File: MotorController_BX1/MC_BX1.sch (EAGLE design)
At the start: 6 parts

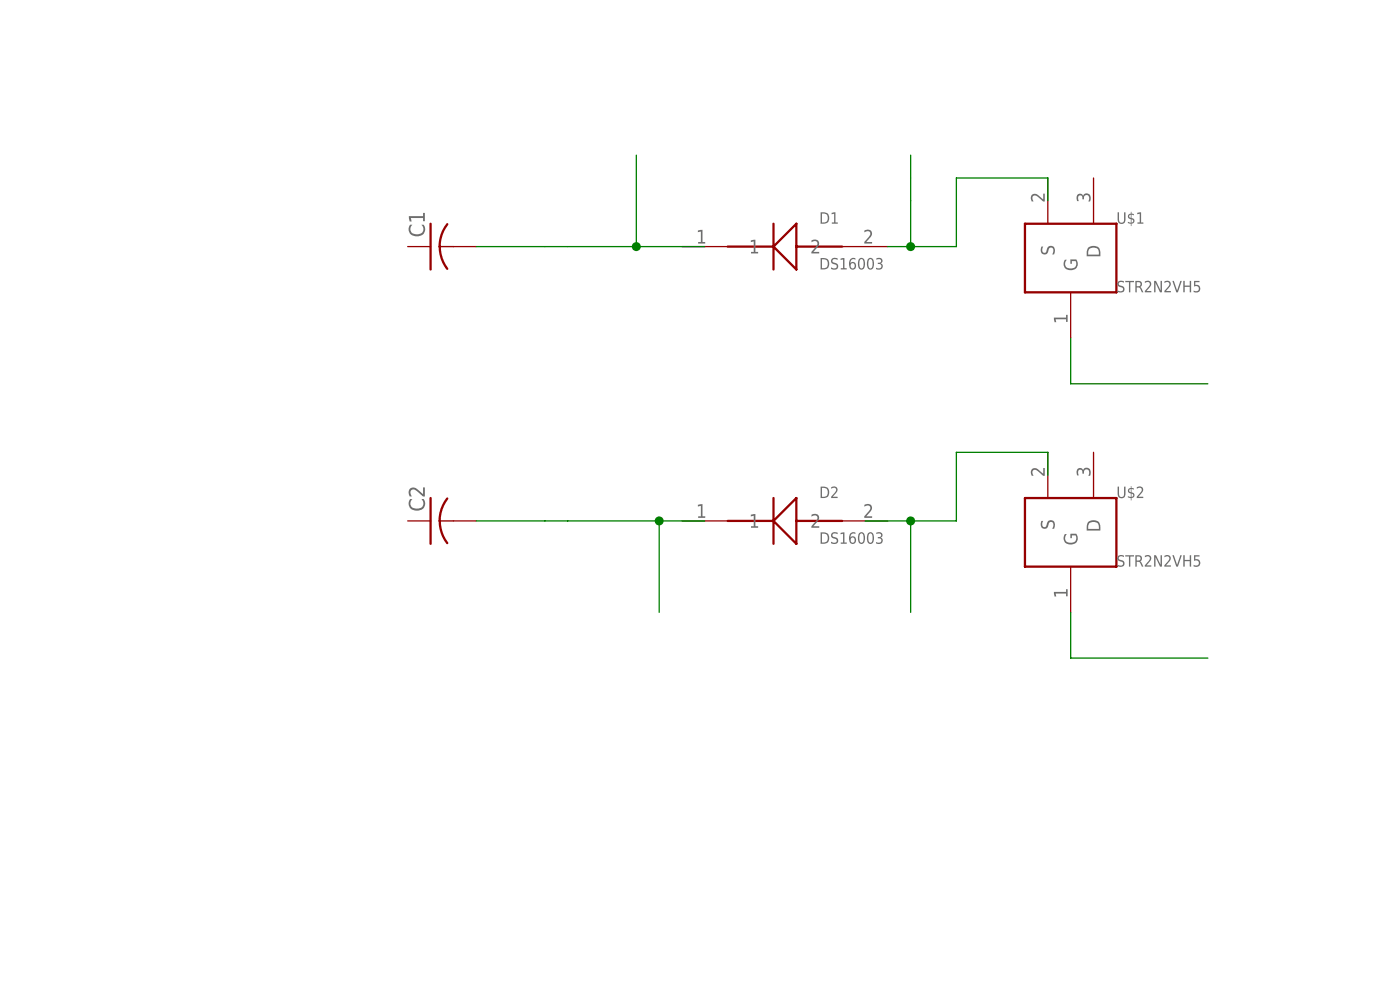
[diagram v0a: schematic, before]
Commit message: Finished first revision of motor controller schematic. Pending: zener shunted to ground, C1 value, and decoupling capacitors from PWM to GND
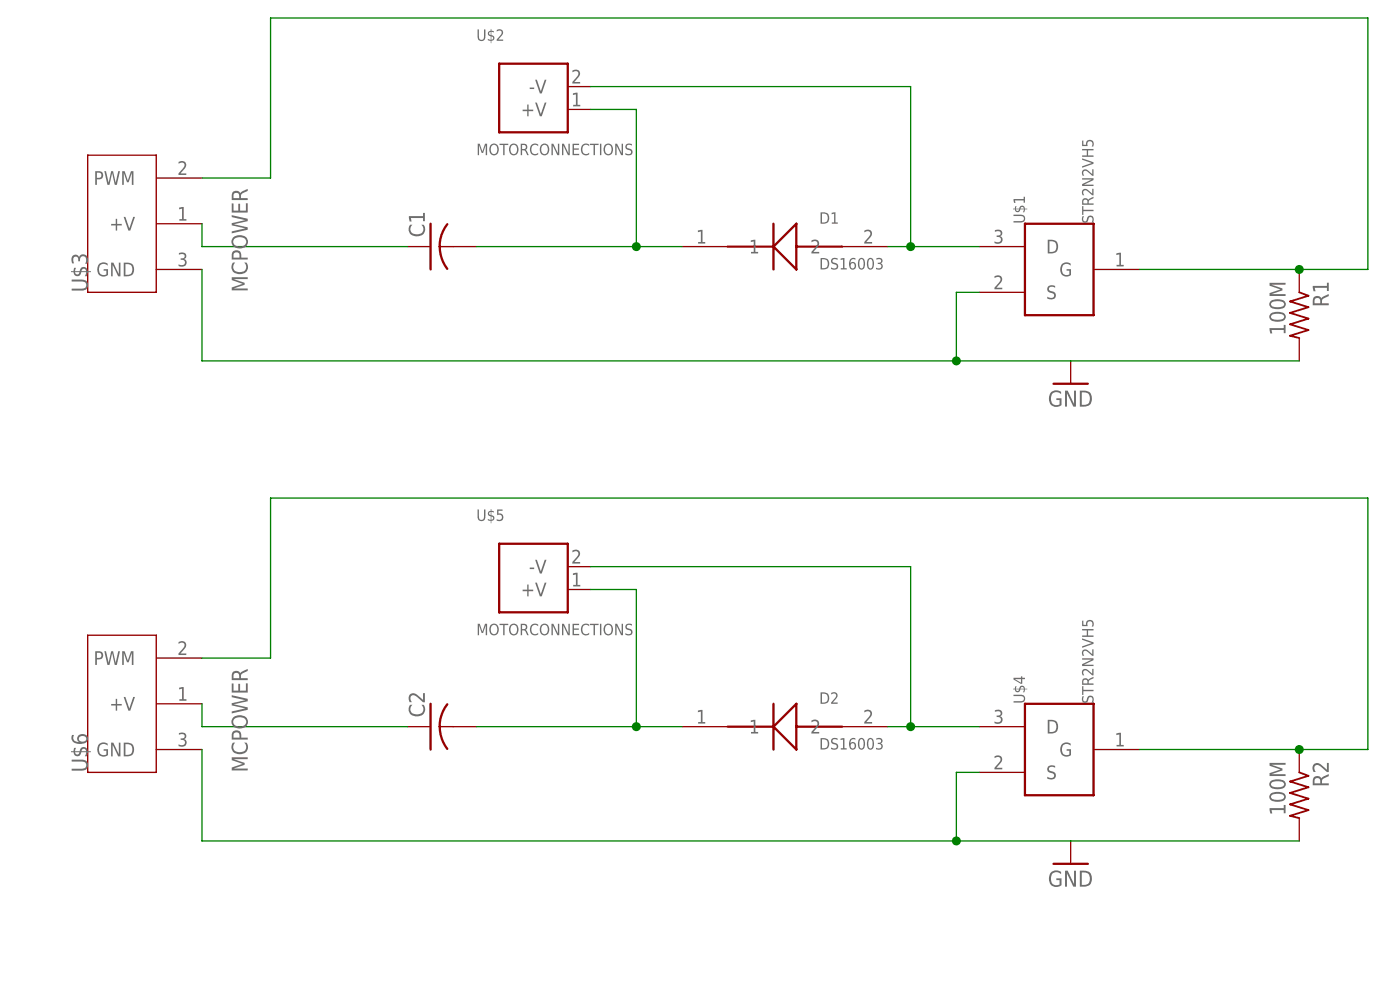
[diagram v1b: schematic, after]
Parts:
- added R1, R2: 100M, rcl:R-US_R0805
- added U$3, U$6: MCPOWER, seds:MCPOWER
- added U$4: STR2N2VH5, seds:STR2N2VH5
- added U$5: MOTORCONNECTIONS, seds:MOTORCONNECTIONS
- U$2: value STR2N2VH5 -> MOTORCONNECTIONS; device seds:STR2N2VH5 -> seds:MOTORCONNECTIONS
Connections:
- removed net N$4: U$2.G
- new net GND: R1.2, R2.2, U$1.S, U$3.GND, U$4.S, U$6.GND
- new net N$7: C2.2, D2.1, U$5.+V
- new net N$8: C1.1, U$3.+V
- new net N$9: C2.1, U$6.+V
- net N$1: now also U$1.D, U$2.-V; no longer U$1.S
- net N$2: now also D2.2, U$4.D, U$5.-V; no longer U$2.S
- net N$3: now also R1.1, U$3.PWM
- net N$5: now also D1.1, U$2.+V
- net N$6: now also R2.1, U$4.G, U$6.PWM; no longer C2.2
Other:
- moved on the sheet: C2, D2, U$1

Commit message: finished board design for BX1 motor controller
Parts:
- C1, C2: value (none) -> 100E-6; device rcl:C-USC0603 -> rcl:C-USC0805
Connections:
- removed net N$7: C2.2, D2.1, U$5.+V
- removed net N$9: C2.1, U$6.+V
- net GND: now also C1.1, C2.1
- net N$5: now also C2.2, D2.1, U$5.+V, U$6.+V; no longer C1.2, D1.1, U$2.+V
- net N$8: now also C1.2, D1.1, U$2.+V; no longer C1.1
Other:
- moved on the sheet: C1, C2, D2, R2, U$4, U$5, U$6
